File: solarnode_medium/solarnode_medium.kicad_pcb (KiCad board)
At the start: 2 copper layers, 77 x 80 mm, 126 parts, among them J1 Conn_01x06, J2 Conn_01x04, Q1 AO3400, Q2 AO3400, Q3 AO3400, Q4 AO3400, Q5 Q_NPN_BEC, Q6 Q_NPN_BEC, Q7 Q_NPN_BEC, Q8 Q_NMOS_GSD, SW1 SW_Push, SW2 SW_Push, SW3 SW_Push, U1 YX59012, U2 SGM2033-3.3, U3 MAX485E, U4 SGM48211, U5 SGM48211, U6 LM358, U7 YX59012, U8 CH32V203C8T6, Y1 Crystal_GND24_Small, Y2 Crystal_Small

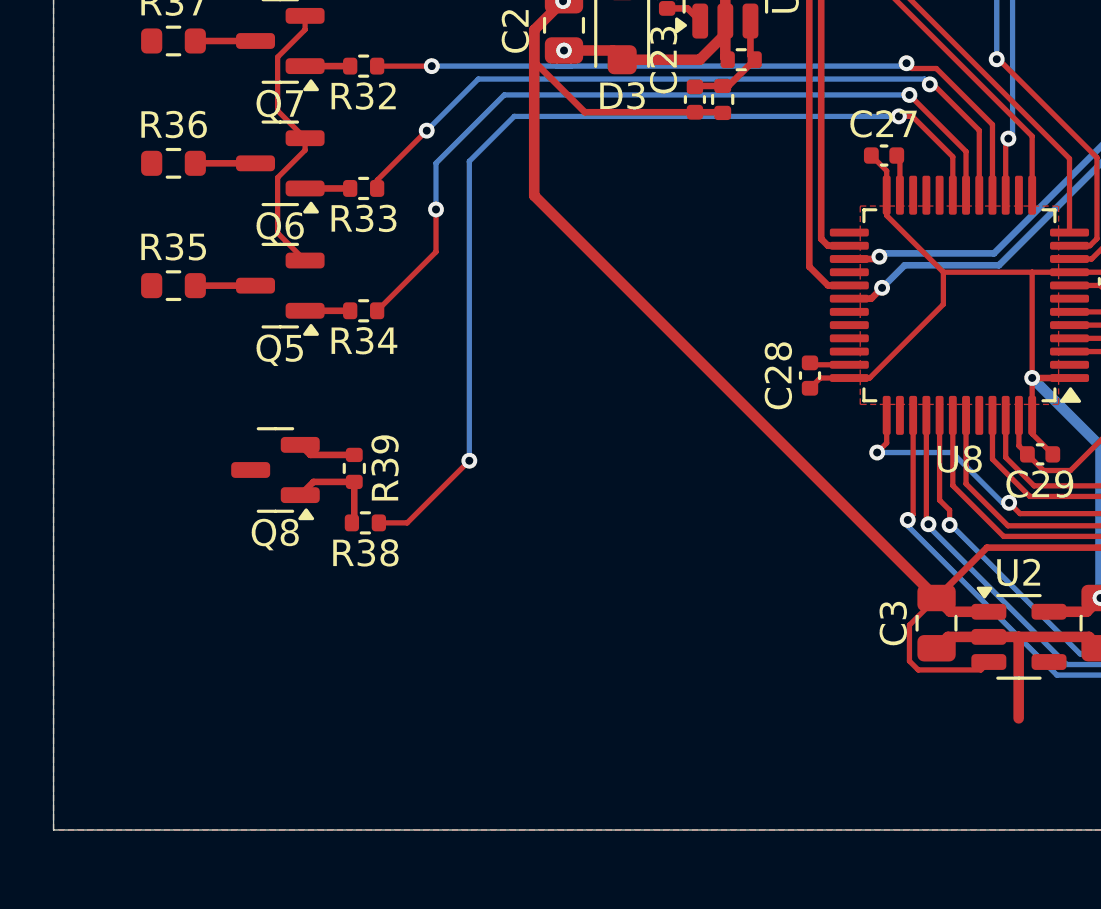
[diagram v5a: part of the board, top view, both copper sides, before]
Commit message: 添加备用电池充电和电源切换电路
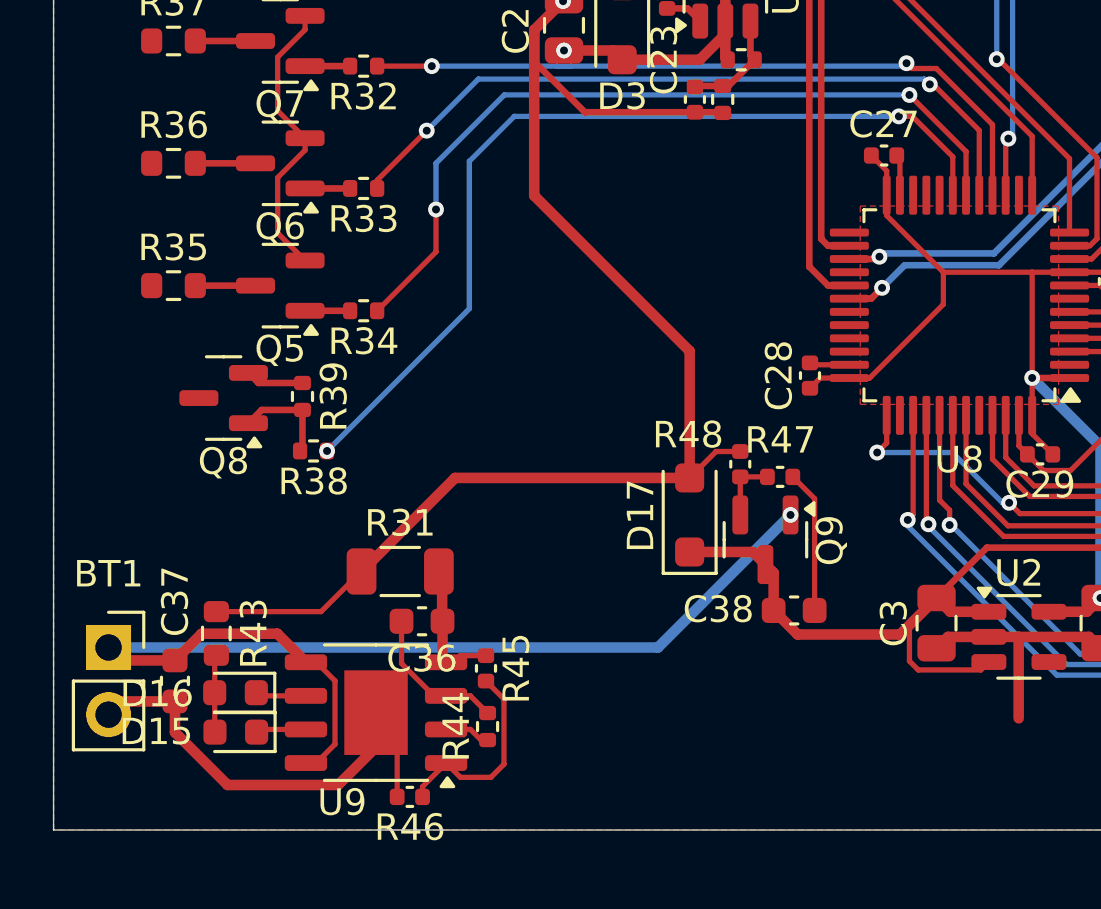
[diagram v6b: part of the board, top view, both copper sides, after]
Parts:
- added BT1: Battery_Cell, Connector_PinSocket_2.54mm:PinSocket_1x02_P2.54mm_Vertical, F.Cu at (71.8, 117.9)
- added C36: 1uf, Capacitor_SMD:C_0603_1608Metric, F.Cu at (83.6, 116.9)
- added C37: 1uf, Capacitor_SMD:C_0603_1608Metric, F.Cu at (74.3, 119.2)
- added C38: C, Capacitor_SMD:C_0603_1608Metric, F.Cu at (97.7, 116.5)
- added D15: LED, LED_SMD:LED_0603_1608Metric, F.Cu at (76.6, 121.1)
- added D16: LED, LED_SMD:LED_0603_1608Metric, F.Cu at (76.6, 119.6)
- added D17: D_Schottky, Diode_SMD:D_SOD-123F, F.Cu at (93.8, 112.9)
- added Q9: PMOS, Package_TO_SOT_SMD:SOT-23, F.Cu at (96.6, 113.8)
- added R31: 0.4, Resistor_SMD:R_1206_3216Metric, F.Cu at (82.8, 115.0)
- added R43: 330, Resistor_SMD:R_0603_1608Metric, F.Cu at (75.9, 117.4)
- added R44: R, Resistor_SMD:R_0402_1005Metric, F.Cu at (86.1, 120.9)
- added R45: R, Capacitor_SMD:C_0402_1005Metric, F.Cu at (86.0, 118.7)
- added R46: R, Capacitor_SMD:C_0402_1005Metric, F.Cu at (83.2, 123.5)
- added R47: 100k, Capacitor_SMD:C_0402_1005Metric, F.Cu at (97.2, 111.5)
- added R48: 1k, Capacitor_SMD:C_0402_1005Metric, F.Cu at (95.7, 111.0)
- added U9: CN3058E, Package_SO:HTSOP-8-1EP_3.9x4.9mm_P1.27mm_EP2.4x3.2mm, F.Cu at (81.9, 120.4)
- moved Q8 3.35 mm to (76.1, 108.5)
- moved R38 3.35 mm to (79.5, 110.5)
- moved R39 3.35 mm to (79.1, 108.4)
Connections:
- C3 pad 1: +5V -> +5VB
- C5 pad 2: +5V -> +5VB
- U2 pad 1: +5V -> +5VB
- U2 pad 3: +5V -> +5VB
- U3 pad 8: +5V -> +5VB
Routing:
- net +5VB: track 0.00 -> 86.6 mm
- net +5V: track 158.1 -> 97.5 mm
- net Net-(BT1-+): track 0.00 -> 41.6 mm, vias 0 -> 1
- net GND: track 283.7 -> 312.6 mm
- net Net-(U9-TEMP): track 0.00 -> 7.69 mm
- net Net-(U9-VIN): track 0.00 -> 5.24 mm
- net Net-(D15-A): track 0.00 -> 2.94 mm
- net /MCU and Commication/SPK: track 36.8 -> 34.2 mm
- net Net-(Q9-G): track 0.00 -> 2.46 mm
- net Net-(D16-K): track 0.00 -> 1.92 mm
- net Net-(D15-K): track 0.00 -> 1.91 mm
- net Net-(U9-ISET): track 0.00 -> 1.70 mm
